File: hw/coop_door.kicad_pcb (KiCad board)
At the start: 2 copper layers, 110 x 110 mm, 53 parts, among them J1 Screw_Terminal_01x02, J2 Screw_Terminal_01x02, J3 Screw_Terminal_01x02, Q1 Q_NMOS_DDGSDD, Q2 IRF4905, Q3 Q_NMOS_DDGSDD, Q4 Q_Dual_NMOS_S1G1D2S2G2D1, Q5 Q_PMOS_DDGSDD, SW1 SW_Push, SW2 SW_DPDT_x2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

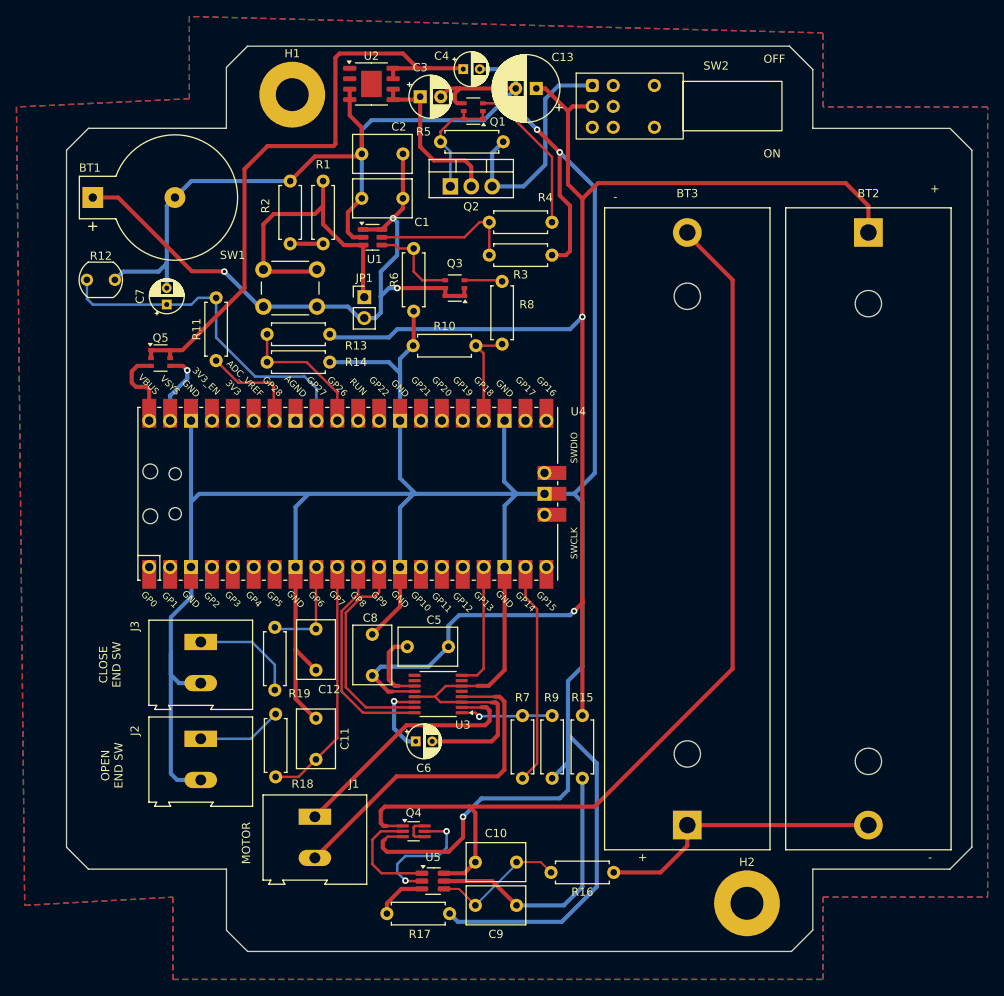
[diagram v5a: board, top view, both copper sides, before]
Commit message: Update schematics&PCB
- Add button to start the battery protection IC
- Add motor resitor to AISEN pin to limit the current to ~300mA
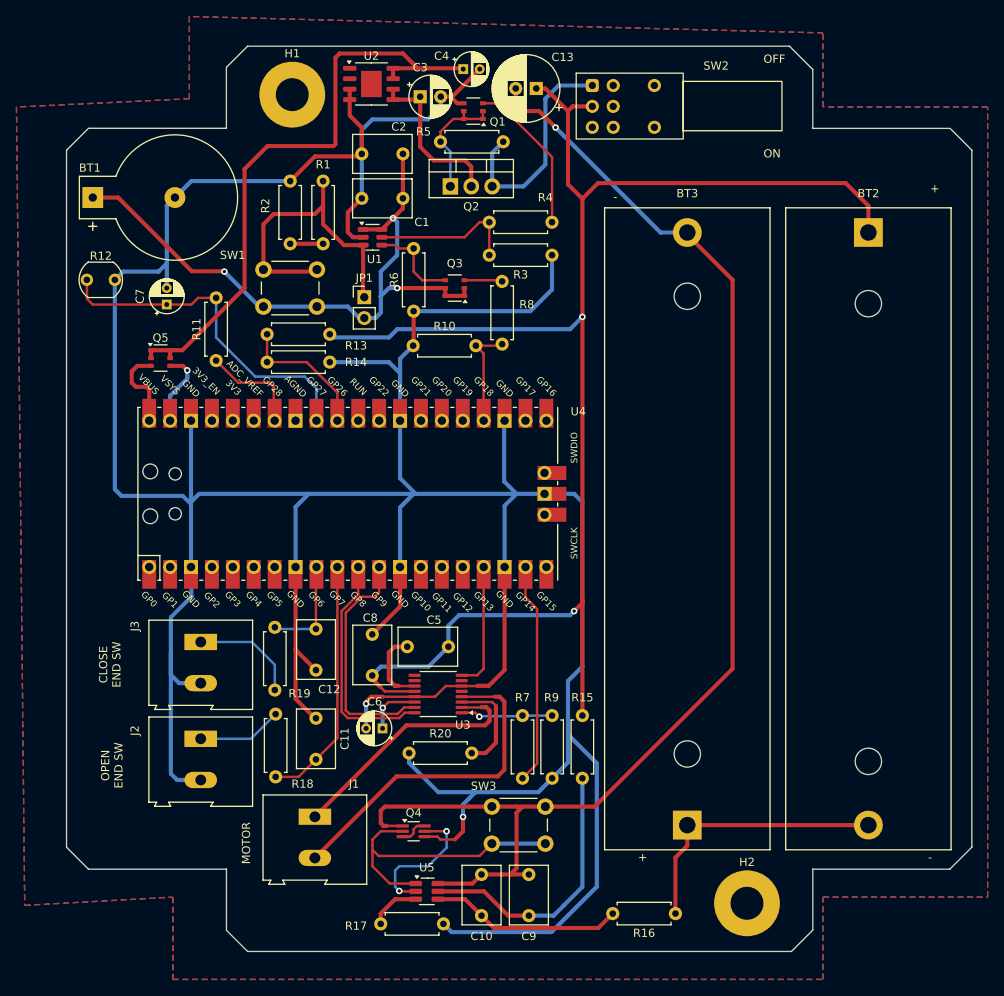
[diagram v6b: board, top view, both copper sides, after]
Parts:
- added R20: 0R68, Resistor_THT:R_Axial_DIN0207_L6.3mm_D2.5mm_P7.62mm_Horizontal, F.Cu at (125.4, 119.5)
- added SW3: SW_Push, Button_Switch_THT:SW_PUSH_6mm, F.Cu at (135.5, 126.0)
- Q1, Q3: value Q_NMOS_DDGSDD -> IRLTS6342
- Q4: value Q_Dual_NMOS_S1G1D2S2G2D1 -> BSD235NH
- Q5: value Q_PMOS_DDGSDD -> BSL207SPH
- moved R16 9.01 mm to (157.8, 139.0)
- moved C10 7.77 mm to (134.2, 139.2), turned to 90 degrees
- moved C6 4.33 mm to (122.2, 116.5), turned to 180 degrees
- moved C9 1.95 mm to (140.0, 139.2), turned to 90 degrees
- moved R17 1.46 mm to (122.0, 140.2)
- moved U5 1.46 mm to (127.6, 136.3)
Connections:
- C13 pad 2: GND -> Net-(BT3--)
- C9 pad 2: Net-(U5-VC) -> Net-(BT3--)
- Q4 pad 3: GND -> Net-(Q4A-D)
- Q4 pad 4: Net-(Q4A-D) -> GND
- U3 pad 3: GND -> /motor_drv_AISEN
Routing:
- net GND: track 538.1 -> 494.7 mm, vias 3 -> 2
- net Net-(BT3--): track 120.9 -> 158.9 mm, vias 0 -> 1
- net Net-(Q4A-G): track 13.5 -> 35.4 mm
- net /motor_drv_AISEN: track 0.00 -> 12.3 mm
- net Net-(U5-VC): track 16.7 -> 23.4 mm
- net Net-(U3-VINT): track 9.20 -> 6.66 mm
- net /motor_drv_AIN2: track 26.6 -> 28.9 mm
- net /motor_drv_AIN1: track 25.9 -> 27.9 mm
- net Net-(BT2--): track 35.1 -> 33.7 mm
- net Net-(U5-VDD): track 32.1 -> 33.4 mm
- net Net-(Q4B-G): track 15.9 -> 16.8 mm
